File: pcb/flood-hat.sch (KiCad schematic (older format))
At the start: 4 parts, among them J1 PI2GPIO, P1 CONN_01X03, P6 CONN_01X03, P7 CONN_01X03

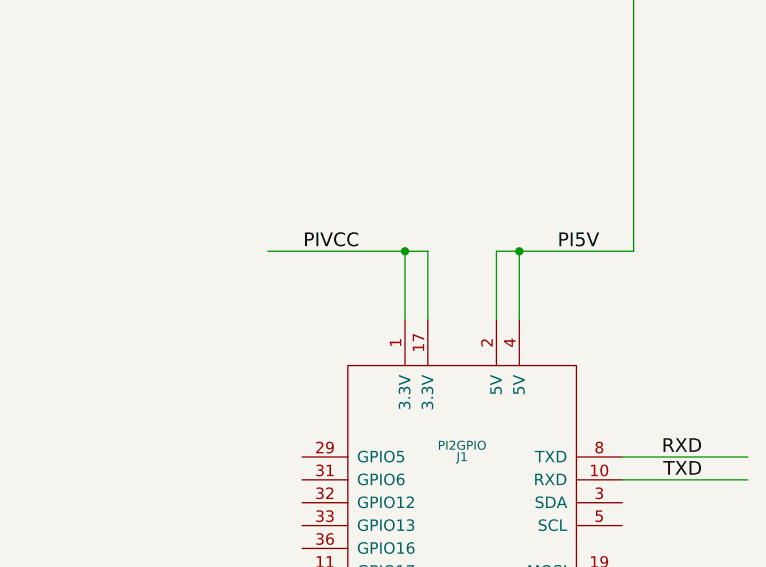
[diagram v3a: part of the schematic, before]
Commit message: PCB simplification
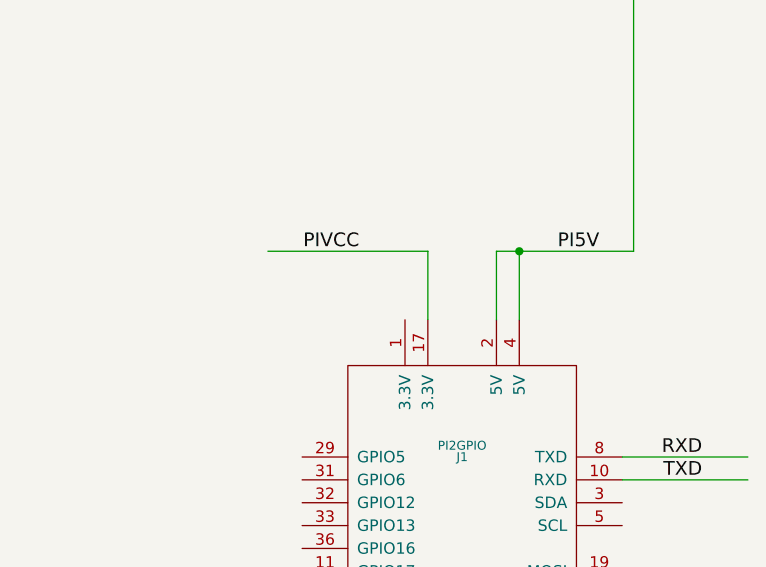
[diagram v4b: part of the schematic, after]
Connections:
- wire segments 50 -> 49
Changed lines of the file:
@@
 	7300 2300 7300 2600
-Wire Wire Line
-	7200 2600 7200 2300
-Connection ~ 7200 2300
 Wire Wire Line
 	7600 2600 7600 2300

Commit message: completed PCB layout first good draft
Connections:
- wire segments 49 -> 50
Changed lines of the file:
@@
 F4 "DHT" I R 3900 6200 60
 F5 "5Vsensor" I L 2750 6200 60
+F6 "PiVCC" I L 2750 6300 60
 $EndSheet
 Wire Wire Line
@@
 Text Notes 4900 6650 0    60   ~ 0
 Solder Bridges
+Wire Wire Line
+	2750 6300 2150 6300
+Text Label 2200 6300 0    60   ~ 0
+PIVCC
 $EndSCHEMATC

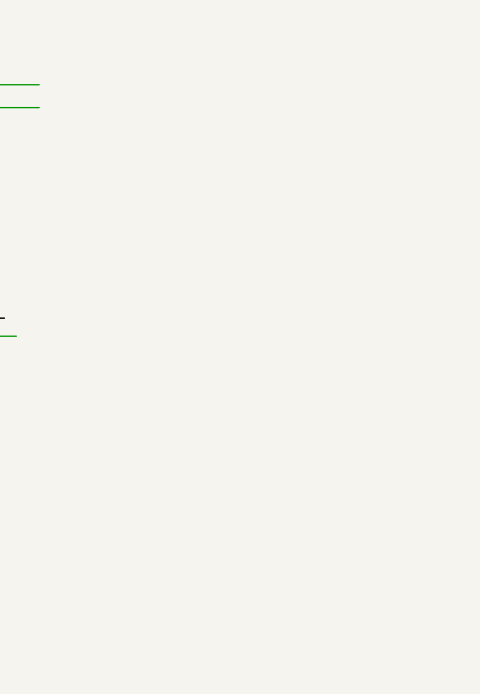
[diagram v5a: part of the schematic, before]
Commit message: added fiducials
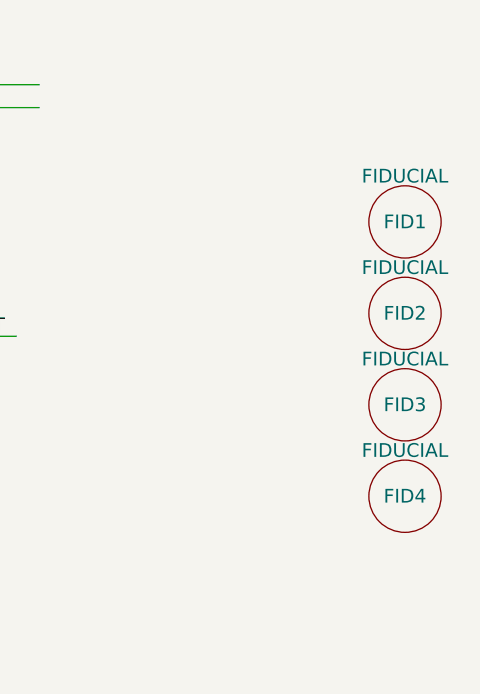
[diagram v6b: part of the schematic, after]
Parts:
- added FID1, FID2, FID3, FID4: FIDUCIAL, smd:FID0.5, symbol FIDUCIAL
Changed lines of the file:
@@
 Text Label 2200 6300 0    60   ~ 0
 PIVCC
+$Comp
+L FIDUCIAL FID1
+U 1 1 580B3E5C
+P 10300 3800
+F 0 "FID1" H 10300 3800 60  0000 C CNN
+F 1 "FIDUCIAL" H 10300 4000 60  0000 C CNN
+F 2 "smd:FID0.5" H 10300 3800 60  0001 C CNN
+F 3 "" H 10300 3800 60  0000 C CNN
+	1    10300 3800
+	1    0    0    -1
+$EndComp
+$Comp
+L FIDUCIAL FID2
+U 1 1 580B3F76
+P 10300 4200
+F 0 "FID2" H 10300 4200 60  0000 C CNN
+F 1 "FIDUCIAL" H 10300 4400 60  0000 C CNN
+F 2 "smd:FID0.5" H 10300 4200 60  0001 C CNN
+F 3 "" H 10300 4200 60  0000 C CNN
+	1    10300 4200
+	1    0    0    -1
+$EndComp
+$Comp
+L FIDUCIAL FID3
+U 1 1 580B402A
+P 10300 4600
+F 0 "FID3" H 10300 4600 60  0000 C CNN
+F 1 "FIDUCIAL" H 10300 4800 60  0000 C CNN
+F 2 "smd:FID0.5" H 10300 4600 60  0001 C CNN
+F 3 "" H 10300 4600 60  0000 C CNN
+	1    10300 4600
+	1    0    0    -1
+$EndComp
+$Comp
+L FIDUCIAL FID4
+U 1 1 580B41D3
+P 10300 5000
+F 0 "FID4" H 10300 5000 60  0000 C CNN
+F 1 "FIDUCIAL" H 10300 5200 60  0000 C CNN
+F 2 "smd:FID0.5" H 10300 5000 60  0001 C CNN
+F 3 "" H 10300 5000 60  0000 C CNN
+	1    10300 5000
+	1    0    0    -1
+$EndComp
 $EndSCHEMATC
